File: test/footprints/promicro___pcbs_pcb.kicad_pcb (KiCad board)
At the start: 2 copper layers, 2 parts

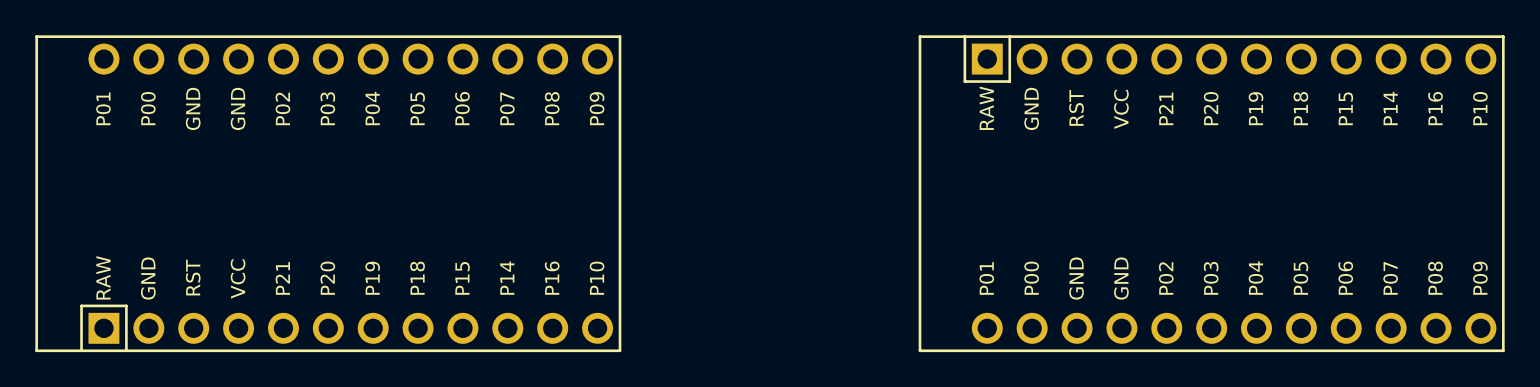
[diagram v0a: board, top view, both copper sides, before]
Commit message: TEST: Fix tests for new power netclass
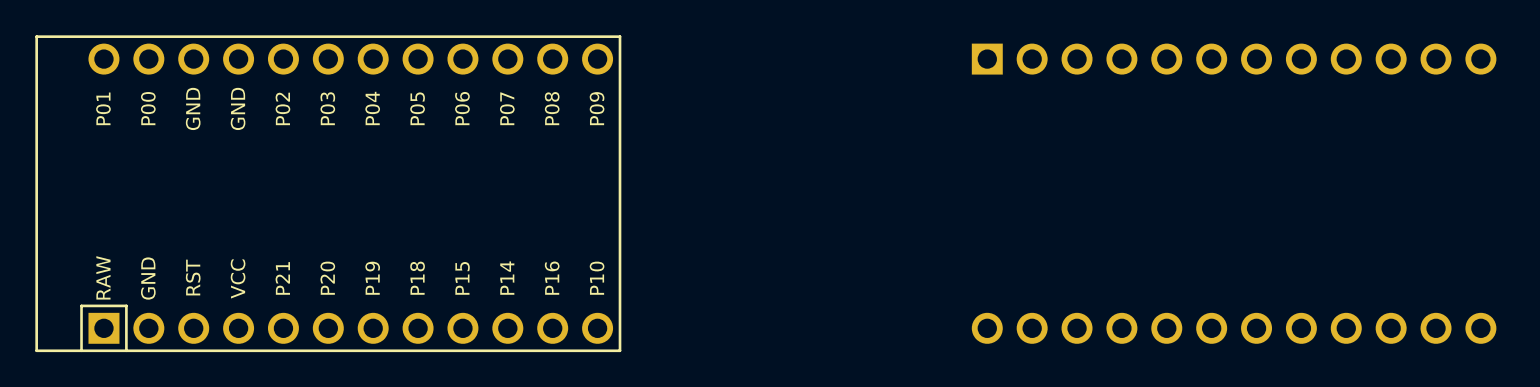
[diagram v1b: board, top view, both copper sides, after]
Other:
- net class Power added: clearance 0.2, trace_width 0.5, via_dia 0.8, via_drill 0.4
